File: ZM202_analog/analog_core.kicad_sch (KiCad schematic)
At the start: 29 parts, among them U3 LM348B, U8 CD4052B

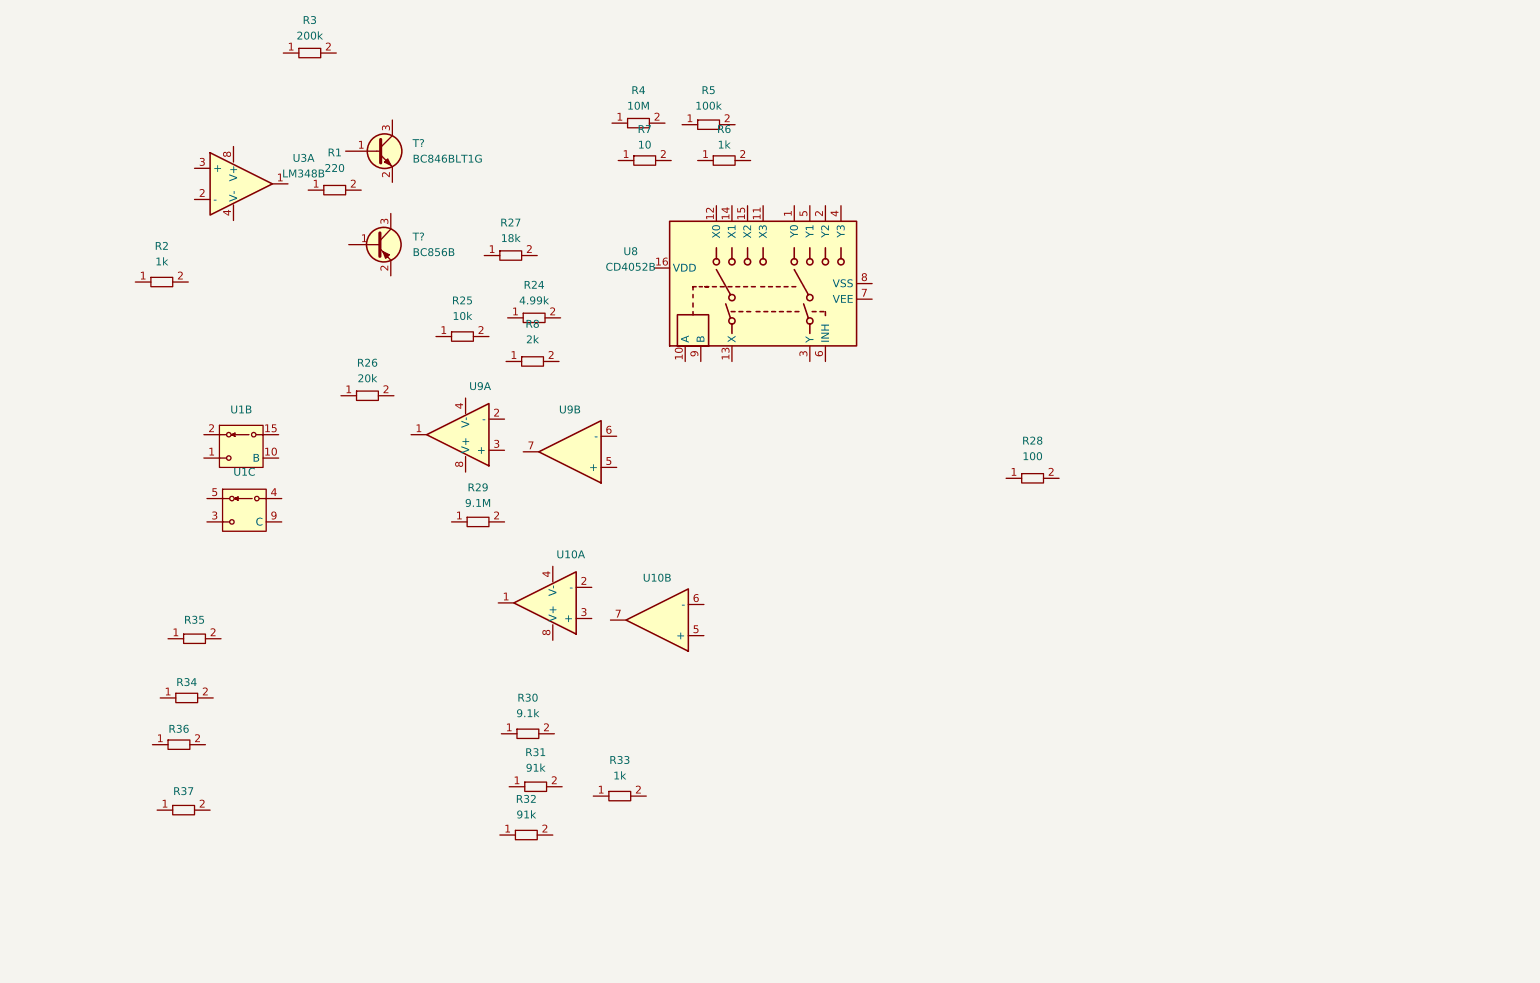
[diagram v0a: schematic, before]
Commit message: Wired analog part.
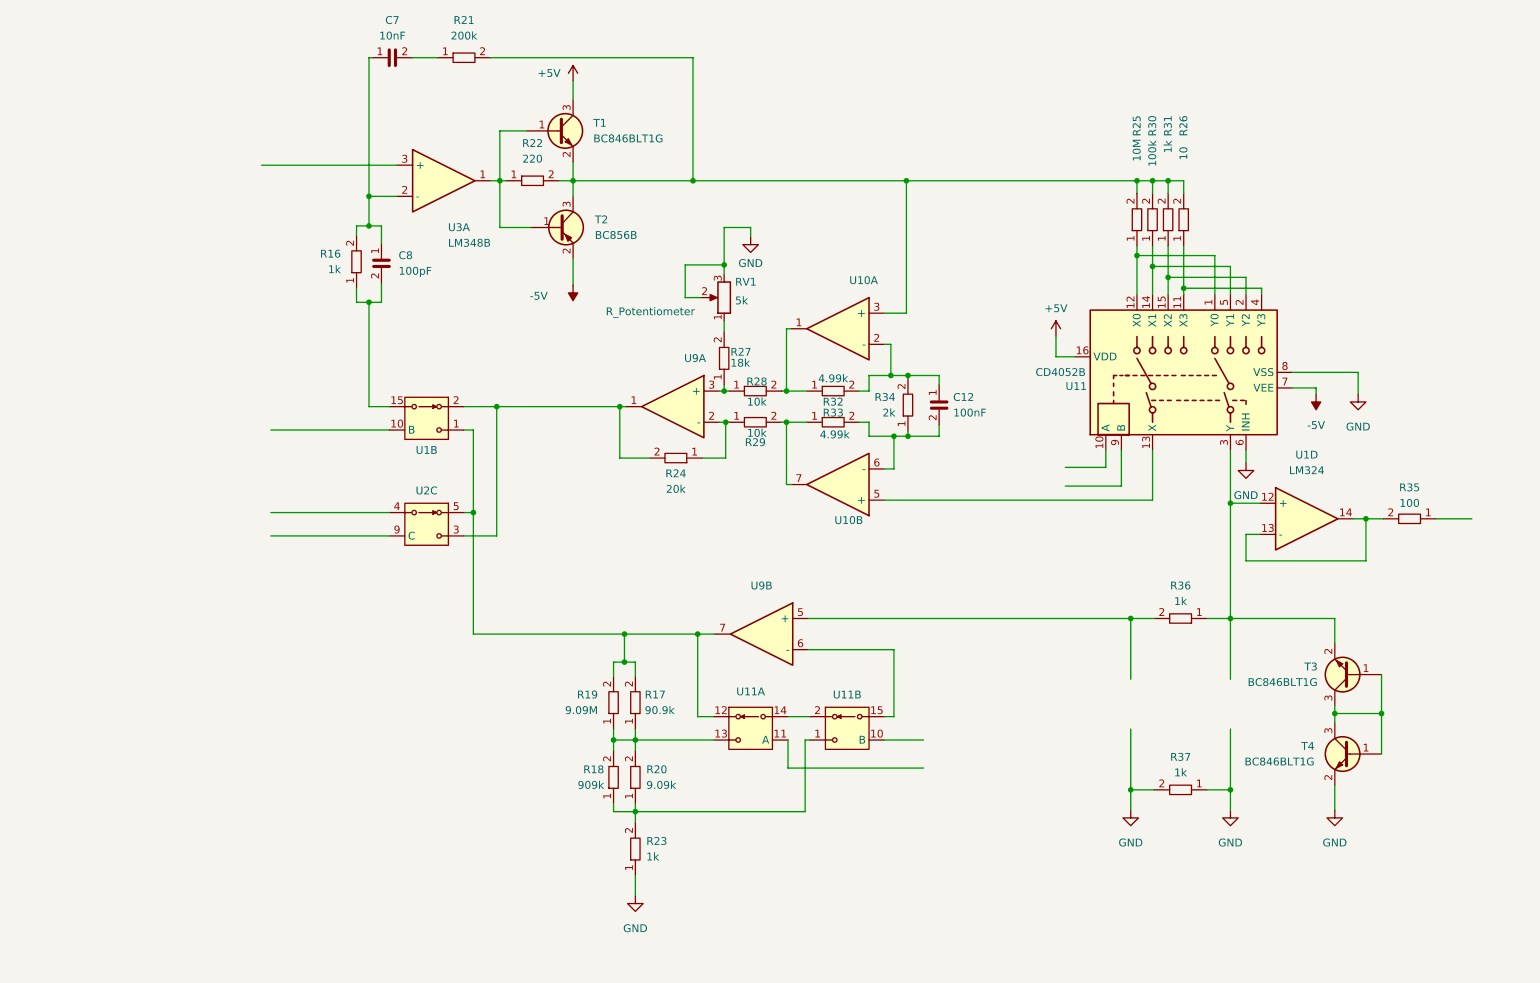
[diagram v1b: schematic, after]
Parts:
- removed R24: R0603_4.99k, Resistor_SMD:R_0603_1608Metric, symbol Jojos_Lib:R0603_4.99k
- removed R25: R0603_10k, Resistor_SMD:R_0603_1608Metric, symbol Jojos_Lib:R0603_10k
- removed R29: R0603_9.1M, Resistor_SMD:R_0603_1608Metric, symbol Jojos_Lib:R0603_9.1M
- removed R30: R0603_9.1k, Resistor_SMD:R_0603_1608Metric, symbol Jojos_Lib:R0603_9.1k
- removed R31, R32: R0603_91k, Resistor_SMD:R_0603_1608Metric, symbol Jojos_Lib:R0603_91k
- removed unit 3 of U1
- removed unit 2 of U9
- added C12: C0603_100nF_25V, Capacitor_SMD:C_0603_1608Metric, symbol Jojos_Lib:C0603_100nF_25V
- added C7: C0603_10nF_50V, Capacitor_SMD:C_0603_1608Metric, symbol Jojos_Lib:C0603_10nF_50V
- added C8: C0603_100pF_50V, Capacitor_SMD:C_0603_1608Metric, symbol Jojos_Lib:C0603_100pF_50V
- added R28, R29: R0603_10k, Resistor_SMD:R_0603_1608Metric, symbol Jojos_Lib:R0603_10k
- added R32, R33: R0603_4.99k, Resistor_SMD:R_0603_1608Metric, symbol Jojos_Lib:R0603_4.99k
- added R36, R37: R0603_1k, Resistor_SMD:R_0603_1608Metric, symbol Jojos_Lib:R0603_1k
- added RV1: R_Potentiometer, Potentiometer_SMD:Potentiometer_Bourns_3214W_Vertical, symbol Jojos_Lib:R_Potentiometer 5k
- added T3, T4: BC846BLT1G, SamacSys_Parts:SOT95P237X111-3N, symbol Jojos_Lib:BC846BLT1G
- added unit 4 of U1
- added unit 2 of U10
- added unit 2 of U11
- added U2: ~, Package_SO:SOIC-16W_5.3x10.2mm_P1.27mm, symbol Jojos_Lib:CD4053
- R17: renamed from R36; Val (none) -> 90.9k
- R18: renamed from R37; Val (none) -> 909k
- R19: renamed from R34; Val (none) -> 9.09M
- R20: renamed from R35; Val (none) -> 9.09k
- gave numbers to parts that had none: 2
- renumbered R2 to R16, R3 to R21, R1 to R22, R33 to R23, R26 to R24, R4 to R25, R7 to R26, R5 to R30, R6 to R31, R8 to R34, R28 to R35, U9 to U10, U8 to U11, U10 to U9
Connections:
- net at U10.1: now also R28.2, R32.1
- net at U10.2 (-): now also R34.2, C12.1, R32.2
- net at U10.3 (+): now also R21.2, R22.2, R25.2, R26.2, R30.2, R31.2, T1.2, T2.3
- net at R24.1: now also U9.2 (-), R29.1
- net at R24.2: now also U1.2, U9.1, U2.3
- net at R27.1: now also U9.3 (+), R28.1
- net at R27.2: now also RV1.1
- net at R22.1: now also T1.1, T2.1, U3.1
- net at R25.1: now also U11.1 (Y0), U11.12 (X0)
- net at R35.2: now also U1.13 (-), U1.14
- net at R31.1: now also U11.15 (X2), U11.2 (Y2)
- net GND: now reaches R23.1
- net GND: now also U11.6 (INH), U11.8 (VSS), R37.1, R37.2, RV1.2, RV1.3, T4.2
- net at R23.2: now also R18.1, R20.1, U11.1
- net at U3.2 (-): now also R16.2, C7.1, C8.1
- net at R17.1: now also R18.2, R19.1, R20.2, U11.13
- net at R17.2: now also R19.2, U1.1, U9.7, U11.12, U2.5
- net +5V: now reaches T1.3
- net +5V: now also U11.16 (VDD)
- net at R26.1: now also U11.11 (X3), U11.4 (Y3)
- net at R16.1: now also U1.15, C8.2
- net -5V: now reaches T2.2
- net -5V: now also U11.7 (VEE)
- net at U9.5 (+): now also R36.2
- net at U9.6 (-): now also U11.15
- net at R30.1: now also U11.14 (X1), U11.5 (Y1)
- net at R34.1: now also C12.2, R33.2, U10.6 (-)
- net at R21.1: now also C7.2
- net at U11.13 (X): now also U10.5 (+)
- net at U11.3 (Y): now also R36.1, T3.2, U1.12 (+)
- new net: T3.1, T3.3, T4.1, T4.3
- new net: R29.2, R33.1, U10.7
- new net: U11.14, U11.2
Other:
- moved on the sheet: R16, R17, R18, R19, R20, R21, R22, R23, R24, R25, R26, R27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

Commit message: Added labels and connections to outside-world.
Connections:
- net V_sig: now reaches R21.2, R22.2, R25.2, R26.2, R30.2, R31.2, T1.2, T2.3, U10.3 (+)
- net DR+: now reaches R36.1, T3.2, U1.12 (+), U11.3 (Y)
- net AVX1: now reaches U11.10 (B)
- net GUARD: now reaches R35.1
- net SN+: now reaches R36.2, U9.5 (+)
- net OSC_IN: now reaches U3.3 (+)
- net VXX: now reaches U2.4
- net C/L: now reaches U2.9 (C)
- net VSRC: now reaches U1.10 (B)
- net AVX0: now reaches U11.11 (A)
- net IX0: now reaches U11.10 (A)
- net IX1: now reaches U11.9 (B)
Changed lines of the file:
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@@
   (junction (at 96.774 37.592) (diameter 0) (color 0 0 0 0)
   )
+  (junction (at 208.28 37.592) (diameter 0) (color 0 0 0 0)
+  )
   (junction (at 133.604 76.962) (diameter 0) (color 0 0 0 0)
   )
@@
     (stroke (width 0) (type default))
   )
+  (wire (pts (xy 208.28 37.592) (xy 228.092 37.592))
+    (stroke (width 0) (type default))
+  )
   (wire (pts (xy 133.35 70.866) (xy 133.35 71.882))
     (stroke (width 0) (type default))
@@
     (stroke (width 0) (type default))
   )
-  (wire (pts (xy 215.9 108.966) (xy 215.9 118.872))
-    (stroke (width 0) (type default))
-  )
   (wire (pts (xy 199.644 136.906) (xy 203.454 136.906))
     (stroke (width 0) (type default))
@@
     (stroke (width 0) (type default))
   )
-  (wire (pts (xy 215.9 127) (xy 215.9 136.906))
+  (wire (pts (xy 215.9 131.318) (xy 215.9 136.906))
     (stroke (width 0) (type default))
   )
@@
     (stroke (width 0) (type default))
   )
-  (wire (pts (xy 199.644 108.966) (xy 199.644 118.872))
+  (wire (pts (xy 199.644 108.966) (xy 199.644 116.332))
     (stroke (width 0) (type default))
   )
@@
     (stroke (width 0) (type default))
   )
+  (wire (pts (xy 215.9 108.966) (xy 215.9 116.332))
+    (stroke (width 0) (type default))
+  )
   (wire (pts (xy 203.2 37.592) (xy 205.74 37.592))
     (stroke (width 0) (type default))
@@
     (stroke (width 0) (type default))
   )
-  (wire (pts (xy 59.436 78.232) (xy 78.74 78.232))
+  (wire (pts (xy 72.898 78.232) (xy 78.74 78.232))
     (stroke (width 0) (type default))
   )
@@
     (stroke (width 0) (type default))
   )
+  (wire (pts (xy 212.09 108.966) (xy 215.9 108.966))
+    (stroke (width 0) (type default))
+  )
+  (wire (pts (xy 75.438 44.958) (xy 77.47 44.958))
+    (stroke (width 0) (type default))
+  )
+  (wire (pts (xy 200.66 48.26) (xy 200.66 49.784))
+    (stroke (width 0) (type default))
+  )
+  (wire (pts (xy 159.512 128.778) (xy 165.862 128.778))
+    (stroke (width 0) (type default))
+  )
+  (wire (pts (xy 92.456 91.694) (xy 92.456 78.232))
+    (stroke (width 0) (type default))
+  )
+  (wire (pts (xy 232.918 113.03) (xy 232.918 108.966))
+    (stroke (width 0) (type default))
+  )
+  (wire (pts (xy 131.572 128.778) (xy 118.872 128.778))
+    (stroke (width 0) (type default))
+  )
+  (wire (pts (xy 133.35 60.452) (xy 133.35 62.23))
+    (stroke (width 0) (type default))
+  )
+  (wire (pts (xy 90.932 95.504) (xy 96.266 95.504))
+    (stroke (width 0) (type default))
+  )
+  (wire (pts (xy 72.898 95.504) (xy 78.74 95.504))
+    (stroke (width 0) (type default))
+  )
+  (wire (pts (xy 129.54 56.642) (xy 127 56.642))
+    (stroke (width 0) (type default))
+  )
+  (wire (pts (xy 218.44 95.25) (xy 218.44 99.568))
+    (stroke (width 0) (type default))
+  )
+  (wire (pts (xy 90.932 74.422) (xy 96.266 74.422))
+    (stroke (width 0) (type default))
+  )
+  (wire (pts (xy 129.032 124.968) (xy 131.572 124.968))
+    (stroke (width 0) (type default))
+  )
+  (wire (pts (xy 232.918 124.46) (xy 240.538 124.46))
+    (stroke (width 0) (type default))
+  )
+  (wire (pts (xy 143.51 71.882) (xy 146.812 71.882))
+    (stroke (width 0) (type default))
+  )
+  (wire (pts (xy 132.588 76.962) (xy 133.604 76.962))
+    (stroke (width 0) (type default))
+  )
   (wire (pts (xy 215.9 90.17) (xy 215.9 108.966))
     (stroke (width 0) (type default))
   )
-  (wire (pts (xy 212.09 108.966) (xy 215.9 108.966))
-    (stroke (width 0) (type default))
-  )
-  (wire (pts (xy 75.438 44.958) (xy 77.47 44.958))
-    (stroke (width 0) (type default))
-  )
-  (wire (pts (xy 200.66 48.26) (xy 200.66 49.784))
-    (stroke (width 0) (type default))
-  )
-  (wire (pts (xy 159.512 128.778) (xy 165.862 128.778))
-    (stroke (width 0) (type default))
-  )
-  (wire (pts (xy 92.456 91.694) (xy 92.456 78.232))
-    (stroke (width 0) (type default))
-  )
-  (wire (pts (xy 232.918 113.03) (xy 232.918 108.966))
-    (stroke (width 0) (type default))
-  )
-  (wire (pts (xy 131.572 128.778) (xy 118.872 128.778))
-    (stroke (width 0) (type default))
-  )
-  (wire (pts (xy 133.35 60.452) (xy 133.35 62.23))
-    (stroke (width 0) (type default))
-  )
-  (wire (pts (xy 90.932 95.504) (xy 96.266 95.504))
-    (stroke (width 0) (type default))
-  )
-  (wire (pts (xy 129.54 56.642) (xy 127 56.642))
-    (stroke (width 0) (type default))
-  )
-  (wire (pts (xy 218.44 95.25) (xy 218.44 99.568))
-    (stroke (width 0) (type default))
-  )
-  (wire (pts (xy 90.932 74.422) (xy 96.266 74.422))
-    (stroke (width 0) (type default))
-  )
-  (wire (pts (xy 129.032 124.968) (xy 131.572 124.968))
-    (stroke (width 0) (type default))
-  )
-  (wire (pts (xy 232.918 124.46) (xy 240.538 124.46))
-    (stroke (width 0) (type default))
-  )
-  (wire (pts (xy 143.51 71.882) (xy 146.812 71.882))
-    (stroke (width 0) (type default))
-  )
-  (wire (pts (xy 132.588 76.962) (xy 133.604 76.962))
-    (stroke (width 0) (type default))
-  )
   (wire (pts (xy 75.438 57.404) (xy 75.438 74.422))
     (stroke (width 0) (type default))
@@
     (stroke (width 0) (type default))
   )
-  (wire (pts (xy 57.912 35.052) (xy 80.01 35.052))
+  (wire (pts (xy 66.04 35.052) (xy 80.01 35.052))
     (stroke (width 0) (type default))
   )
@@
     (stroke (width 0) (type default))
   )
-  (wire (pts (xy 78.74 91.694) (xy 59.436 91.694))
+  (wire (pts (xy 78.74 91.694) (xy 72.898 91.694))
     (stroke (width 0) (type default))
   )
@@
     (stroke (width 0) (type default))
   )
-  (wire (pts (xy 199.644 127) (xy 199.644 136.906))
+  (wire (pts (xy 199.644 131.318) (xy 199.644 136.906))
     (stroke (width 0) (type default))
   )
@@
     (stroke (width 0) (type default))
   )
-  (wire (pts (xy 59.436 95.504) (xy 78.74 95.504))
-    (stroke (width 0) (type default))
-  )
   (wire (pts (xy 73.406 57.404) (xy 75.438 57.404))
     (stroke (width 0) (type default))
@@
     (stroke (width 0) (type default))
   )
+  (hierarchical_label "VSRC" (shape input) (at 72.898 78.232 180) (fields_autoplaced)
+    (effects (font (size 1.27 1.27)) (justify right))
+  )
+  (hierarchical_label "IX1" (shape input) (at 188.976 87.376 180) (fields_autoplaced)
+    (effects (font (size 1.27 1.27)) (justify right))
+  )
+  (hierarchical_label "OSC_IN" (shape input) (at 66.04 35.052 180) (fields_autoplaced)
+    (effects (font (size 1.27 1.27)) (justify right))
+  )
+  (hierarchical_label "AVX1" (shape input) (at 165.862 128.778 0) (fields_autoplaced)
+    (effects (font (size 1.27 1.27)) (justify left))
+  )
+  (hierarchical_label "SN-" (shape input) (at 199.644 131.318 90) (fields_autoplaced)
+    (effects (font (size 1.27 1.27)) (justify left))
+  )
+  (hierarchical_label "DR+" (shape input) (at 215.9 116.332 270) (fields_autoplaced)
+    (effects (font (size 1.27 1.27)) (justify right))
+  )
+  (hierarchical_label "AVX0" (shape input) (at 165.862 133.35 0) (fields_autoplaced)
+    (effects (font (size 1.27 1.27)) (justify left))
+  )
+  (hierarchical_label "IX0" (shape input) (at 188.976 84.328 180) (fields_autoplaced)
+    (effects (font (size 1.27 1.27)) (justify right))
+  )
+  (hierarchical_label "V_sig" (shape input) (at 228.092 37.592 0) (fields_autoplaced)
+    (effects (font (size 1.27 1.27)) (justify left))
+  )
+  (hierarchical_label "SN+" (shape input) (at 199.644 116.332 270) (fields_autoplaced)
+    (effects (font (size 1.27 1.27)) (justify right))
+  )
+  (hierarchical_label "GUARD" (shape input) (at 255.27 92.71 0) (fields_autoplaced)
+    (effects (font (size 1.27 1.27)) (justify left))
+  )
+  (hierarchical_label "VXX" (shape input) (at 72.898 91.694 180) (fields_autoplaced)
+    (effects (font (size 1.27 1.27)) (justify right))
+  )
+  (hierarchical_label "C{slash}L" (shape input) (at 72.898 95.504 180) (fields_autoplaced)
+    (effects (font (size 1.27 1.27)) (justify right))
+  )
+  (hierarchical_label "DR-" (shape input) (at 215.9 131.318 90) (fields_autoplaced)
+    (effects (font (size 1.27 1.27)) (justify left))
+  )
   (symbol (lib_id "Jojos_Lib:TLC2272CD") (at 153.924 61.722 0) (mirror y) (unit 1)

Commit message: Labels everywhere and connected hierarchical sheets.
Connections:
- net VIX: now reaches R24.2, U1.2, U2.3, U9.1
- net VVX: now reaches R17.2, R19.2, U1.1, U11.12, U2.5, U9.7
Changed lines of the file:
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@@
   (junction (at 203.2 37.592) (diameter 0) (color 0 0 0 0)
   )
+  (junction (at 106.172 74.422) (diameter 0) (color 0 0 0 0)
+  )
   (junction (at 75.438 44.958) (diameter 0) (color 0 0 0 0)
   )
@@
   (junction (at 116.332 74.422) (diameter 0) (color 0 0 0 0)
   )
+  (junction (at 106.172 111.506) (diameter 0) (color 0 0 0 0)
+  )
   (junction (at 200.66 49.784) (diameter 0) (color 0 0 0 0)
   )
@@
     (stroke (width 0) (type default))
   )
+  (wire (pts (xy 106.172 74.422) (xy 116.332 74.422))
+    (stroke (width 0) (type default))
+  )
   (wire (pts (xy 232.918 136.144) (xy 232.918 140.208))
     (stroke (width 0) (type default))
@@
     (stroke (width 0) (type default))
   )
+  (wire (pts (xy 106.172 107.442) (xy 106.172 111.506))
+    (stroke (width 0) (type default))
+  )
   (wire (pts (xy 129.032 124.968) (xy 131.572 124.968))
     (stroke (width 0) (type default))
@@
     (stroke (width 0) (type default))
   )
+  (wire (pts (xy 106.172 70.866) (xy 106.172 74.422))
+    (stroke (width 0) (type default))
+  )
   (wire (pts (xy 132.588 76.962) (xy 133.604 76.962))
     (stroke (width 0) (type default))
@@
     (stroke (width 0) (type default))
   )
+  (wire (pts (xy 106.172 111.506) (xy 117.094 111.506))
+    (stroke (width 0) (type default))
+  )
   (wire (pts (xy 75.438 57.404) (xy 75.438 74.422))
     (stroke (width 0) (type default))
@@
     (stroke (width 0) (type default))
   )
-  (wire (pts (xy 96.266 74.422) (xy 116.332 74.422))
+  (wire (pts (xy 96.266 74.422) (xy 106.172 74.422))
     (stroke (width 0) (type default))
   )
@@
     (stroke (width 0) (type default))
   )
-  (wire (pts (xy 92.456 111.506) (xy 117.094 111.506))
+  (wire (pts (xy 92.456 111.506) (xy 106.172 111.506))
     (stroke (width 0) (type default))
   )
@@
     (effects (font (size 1.27 1.27)) (justify right))
   )
+  (hierarchical_label "VVX" (shape input) (at 106.172 107.442 90) (fields_autoplaced)
+    (effects (font (size 1.27 1.27)) (justify left))
+  )
   (hierarchical_label "OSC_IN" (shape input) (at 66.04 35.052 180) (fields_autoplaced)
     (effects (font (size 1.27 1.27)) (justify right))
@@
     (effects (font (size 1.27 1.27)) (justify left))
   )
+  (hierarchical_label "VIX" (shape input) (at 106.172 70.866 90) (fields_autoplaced)
+    (effects (font (size 1.27 1.27)) (justify left))
+  )

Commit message: Connected hierarchical outlets to connector.
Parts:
- added C17 (x2): C0603_100nF_25V, Capacitor_SMD:C_0603_1608Metric, symbol Jojos_Lib:C0603_100nF_25V
- added U4: ~, Package_SO:SOIC-16W_5.3x10.2mm_P1.27mm, symbol Jojos_Lib:CD4053
- added unit 3 of U7
- added unit 3 of U9
- renumbered C8 to C7, C7 to C8, C12 to C9, R21 to R17, R22 to R18, R18 to R20, R17 to R21, R20 to R22, R27 to R25, R28 to R26, R29 to R27, R32 to R28, R33 to R29, R34 to R30, R25 to R31, R30 to R32, R31 to R33, R36 to R34, R37 to R35, R26 to R36, R35 to R37, U3 to U10, U9 to U7, U10 to U9
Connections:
- net +5V: now also C17.2, C17.2, U4.16 (VDD), U7.4 (-), U9.8 (+)
- net -5V: now also C17.1, C17.1, U4.7 (VEE), U7.8 (+), U9.4 (-)
- net GND: now also U4.6 (INH), U4.8 (VSS)

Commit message: Changed amplification resistor/cap in the analog core to 82nF/2.49k and did some various changes in the symbols and updated them into the schematic. Added PWR-flags
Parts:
- removed U10: LM348B, Package_SO:SO-8_3.9x4.9mm_P1.27mm, symbol Jojos_Lib:LM348B
- added C17: C0603_100nF_25V, Capacitor_SMD:C_0603_1608Metric, symbol Jojos_Lib:C0603_100nF_25V
- added U7: LM358B, Package_SO:SO-8_3.9x4.9mm_P1.27mm, symbol Jojos_Lib:LM358B
- C12: renamed from C9; value C0603_100nF_25V -> C0603_82nF_25V; symbol Jojos_Lib:C0603_100nF_25V -> Jojos_Lib:C0603_82nF_25V; Digi-Key 732-7989-1-ND -> (none); Mouser Part Number 710-885012206071 -> CC0603KRX7R9BB823; Price 0.04 -> (none); Val 100nF -> 82nF
- R30: value R0603_2k -> R0603_2.49k; symbol Jojos_Lib:R0603_2k -> Jojos_Lib:R0603_2.49k; Manufacturer_Part_Number RC0603JR-102KL -> CR0603FX-2491ELF; Mouser Part Number 603-RC0603JR-102KL -> 652-CR0603FX-2491ELF; Val 2k -> 2.49k
- U10: renamed from U9; value ~ -> TLC2272
- U8: renamed from U7; value ~ -> TLC2272
- renumbered C8 to C10, C7 to C9, U9 to U10, U7 to U8
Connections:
- net +5V: now also U8.8 (+), C17.2, U7.8 (+); no longer U8.4 (-)
- net -5V: now also U8.4 (-), C17.1, U7.4 (-); no longer U8.8 (+)
- net OSC_IN: now also U7.3 (+)
- net at C10.1, C9.1, R16.2: now also U7.2 (-)
- net at R18.1, T1.1, T2.1: now also U7.1
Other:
- moved on the sheet: U8C
